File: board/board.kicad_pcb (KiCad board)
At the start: 2 copper layers, 42.6 x 75.4 mm, 23 parts, among them J1 port attiny, J10 BMS Bat +, J11 BMS Bat gnd, J12 BMS out -, J13 BMS in +5v, J14 BMS in gnd, J15 alim mp3 -, J17 next, J18 vol -, J2 Conn_01x02_Pin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

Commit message: ajout etiquette global + plan de masse
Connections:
- net Net-(J1-Pin_1) renamed Next + mp3
- net Net-(J1-Pin_3) renamed vol - mp3
- net Net-(J1-Pin_4) renamed bouton NEXT
- net Net-(J1-Pin_5) renamed bouton VOL -
- net Net-(J11-Pin_1) renamed bat +
- net Net-(J12-Pin_1) renamed BMS out -
- net Net-(J13-Pin_1) renamed BMS in +
- net Net-(J14-Pin_1) renamed BMS in gnd
- net Net-(J24-Pin_2) renamed bat gnd
- net Net-(J24-Pin_5) renamed on/off out
- net Net-(J24-Pin_6) renamed on/off in
- net Net-(J24-Pin_7) renamed HP +
- net Net-(J24-Pin_8) renamed HP -
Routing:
- net bat gnd: vias 2 -> 1
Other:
- board text added: "Step up 1A 5V"

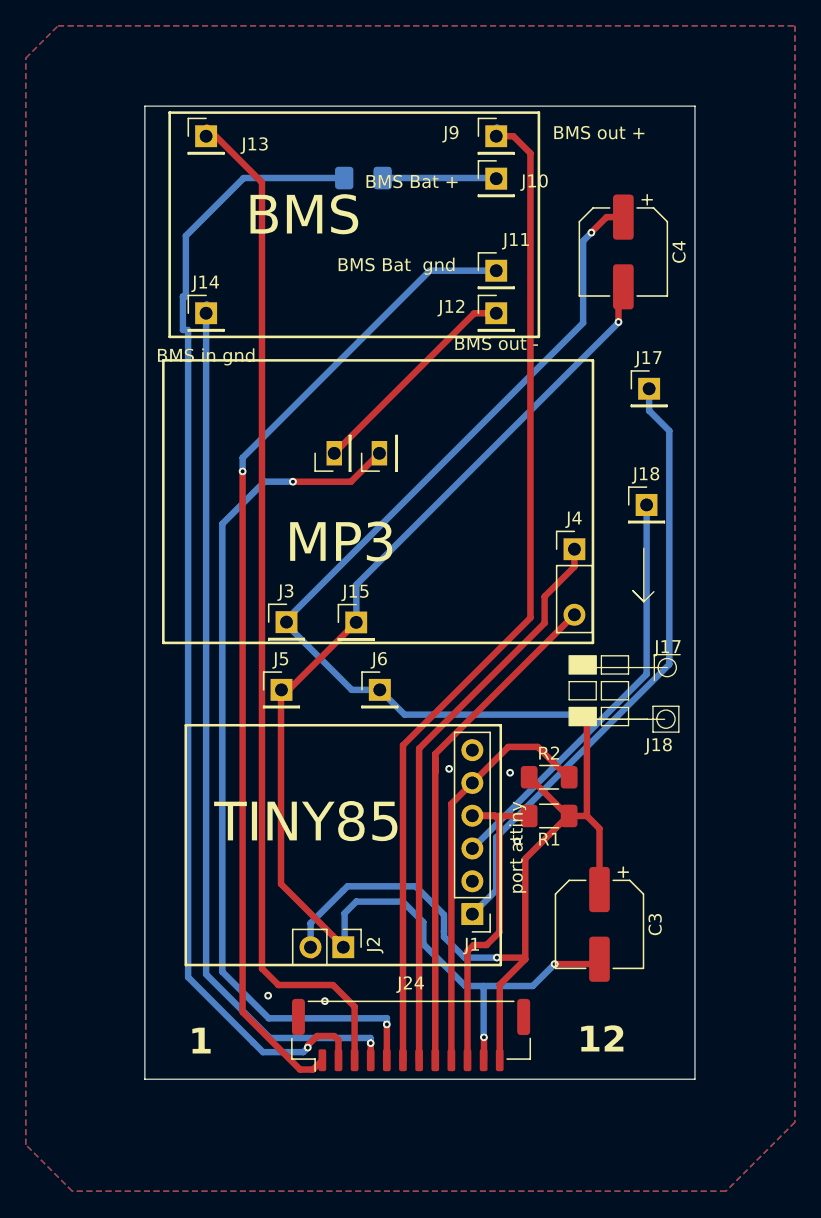
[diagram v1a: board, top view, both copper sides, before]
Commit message: ajout empreinte STM8 + CH32V0003
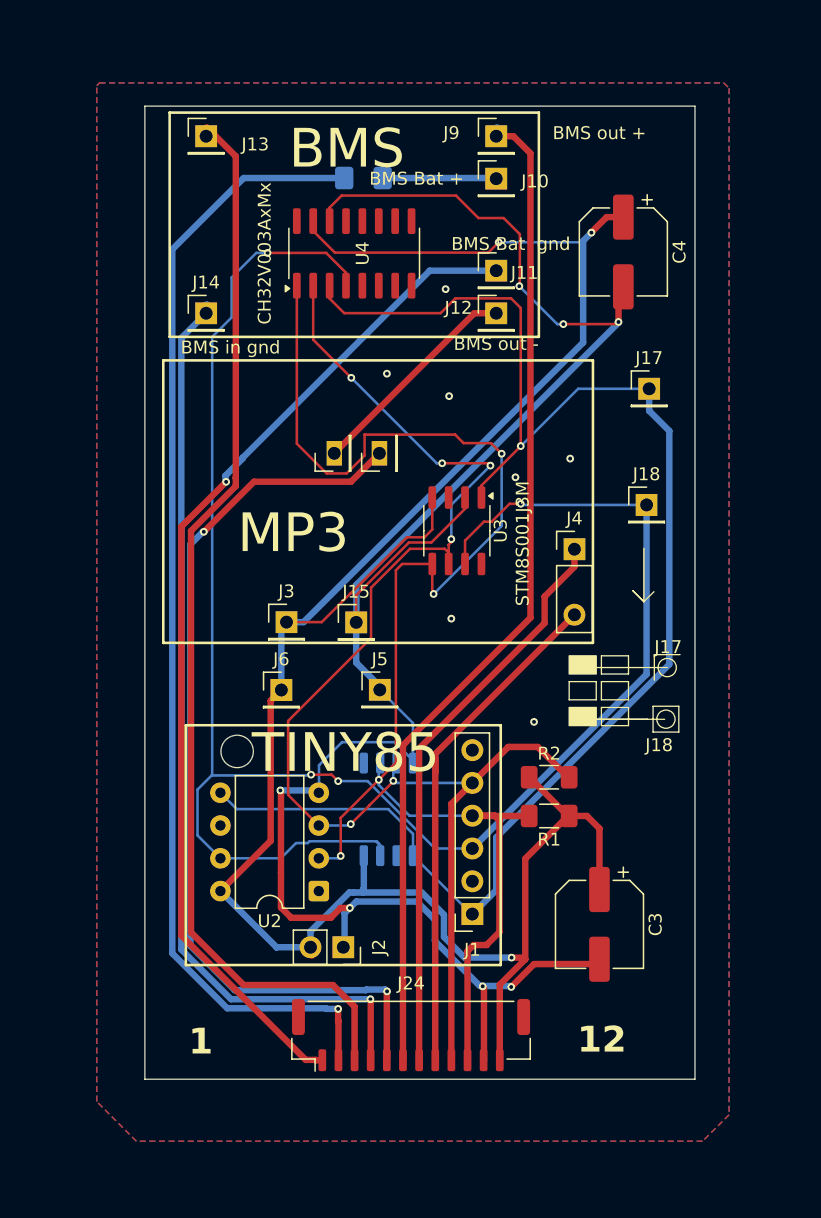
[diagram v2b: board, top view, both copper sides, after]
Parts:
- added U1: ATtiny85-20S, Package_SO:SOIC-8_5.3x5.3mm_P1.27mm, B.Cu at (82.4, 93.5)
- added U2: ATtiny85V-10P, Package_DIP:DIP-8_W7.62mm, F.Cu at (77.0, 99.8)
- added U3: STM8S001J3M, Package_SO:SO-8_3.9x4.9mm_P1.27mm, F.Cu at (87.7, 71.9)
- added U4: CH32V003AxMx, Package_SO:SOP-16_3.9x9.9mm_P1.27mm, F.Cu at (79.7, 50.4)
- J1: footprint Connector_PinHeader_2.54mm:PinHeader_1x06_P2.54mm_Vertical -> Connector_PinSocket_2.54mm:PinSocket_1x06_P2.54mm_Vertical
- J2: footprint Connector_PinHeader_2.54mm:PinHeader_1x02_P2.54mm_Vertical -> Connector_PinSocket_2.54mm:PinSocket_1x02_P2.54mm_Vertical
- moved J6 7.63 mm to (74.1, 84.2)
- moved J5 7.62 mm to (81.7, 84.2)
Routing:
- net vol - mp3: track 32.2 -> 144.2 mm, vias 0 -> 4
- net bouton NEXT: track 26.9 -> 113.0 mm, vias 0 -> 4
- net bouton VOL -: track 31.7 -> 107.9 mm, vias 0 -> 6
- net Next + mp3: track 47.7 -> 116.9 mm, vias 0 -> 1
- net GND: track 98.3 -> 154.2 mm, vias 8 -> 14
- net VCC: track 133.7 -> 175.5 mm
- net BMS in +: track 79.5 -> 84.0 mm
- net on/off out: track 66.6 -> 70.8 mm
- net BMS in gnd: track 68.2 -> 71.5 mm
- net bat +: track 76.9 -> 79.6 mm
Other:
- outline, holes or cut-outs redrawn
- board text added: "Vcc"
- board text added: "gnd"
